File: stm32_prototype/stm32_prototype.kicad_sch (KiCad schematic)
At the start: 16 parts, among them SW1 SW_SPDT, U1 STM32F103C8Tx, Y1 16Mhz

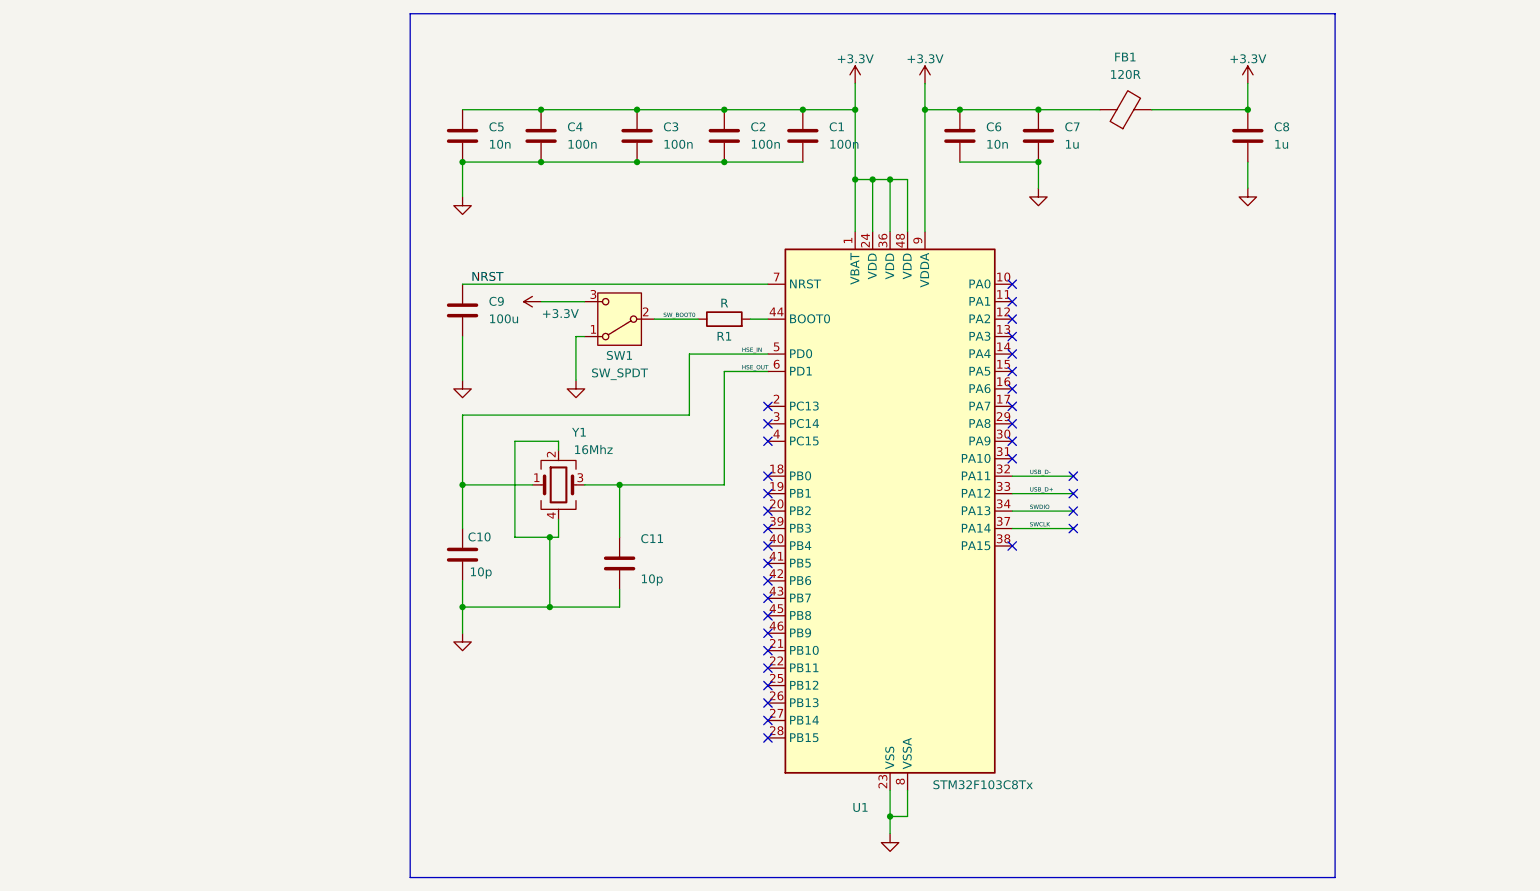
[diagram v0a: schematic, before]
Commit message: Rev B schematic: hierarchical sheets with USB-C, LDO, ESD, debug, Qwiic, Blue-Pill headers
- Split into mcu / power_usb / connectors sheets
- MCU: 8 MHz HSE (15 pF), optional LSE (DNP), BOOT0/RESET buttons, BOOT1 pull-down,
  NRST 100 nF (was 100 uF), VDDA on its own net behind FB1, VBAT solder jumper
- USB-C device (5.1k CC), USBLC6-2SC6, 500 mA PTC, B5819W, AP2112K-3.3
- Cortex-Debug 10-pin, SWD 1x4, Qwiic with jumper-cut 4.7k pull-ups, 2x 1x20 headers
- Footprints, LCSC and MPN on every part; ERC 0 errors / 0 warnings

Co-Authored-By: Claude Opus 5.5 (1M context) <noreply@anthropic.com>
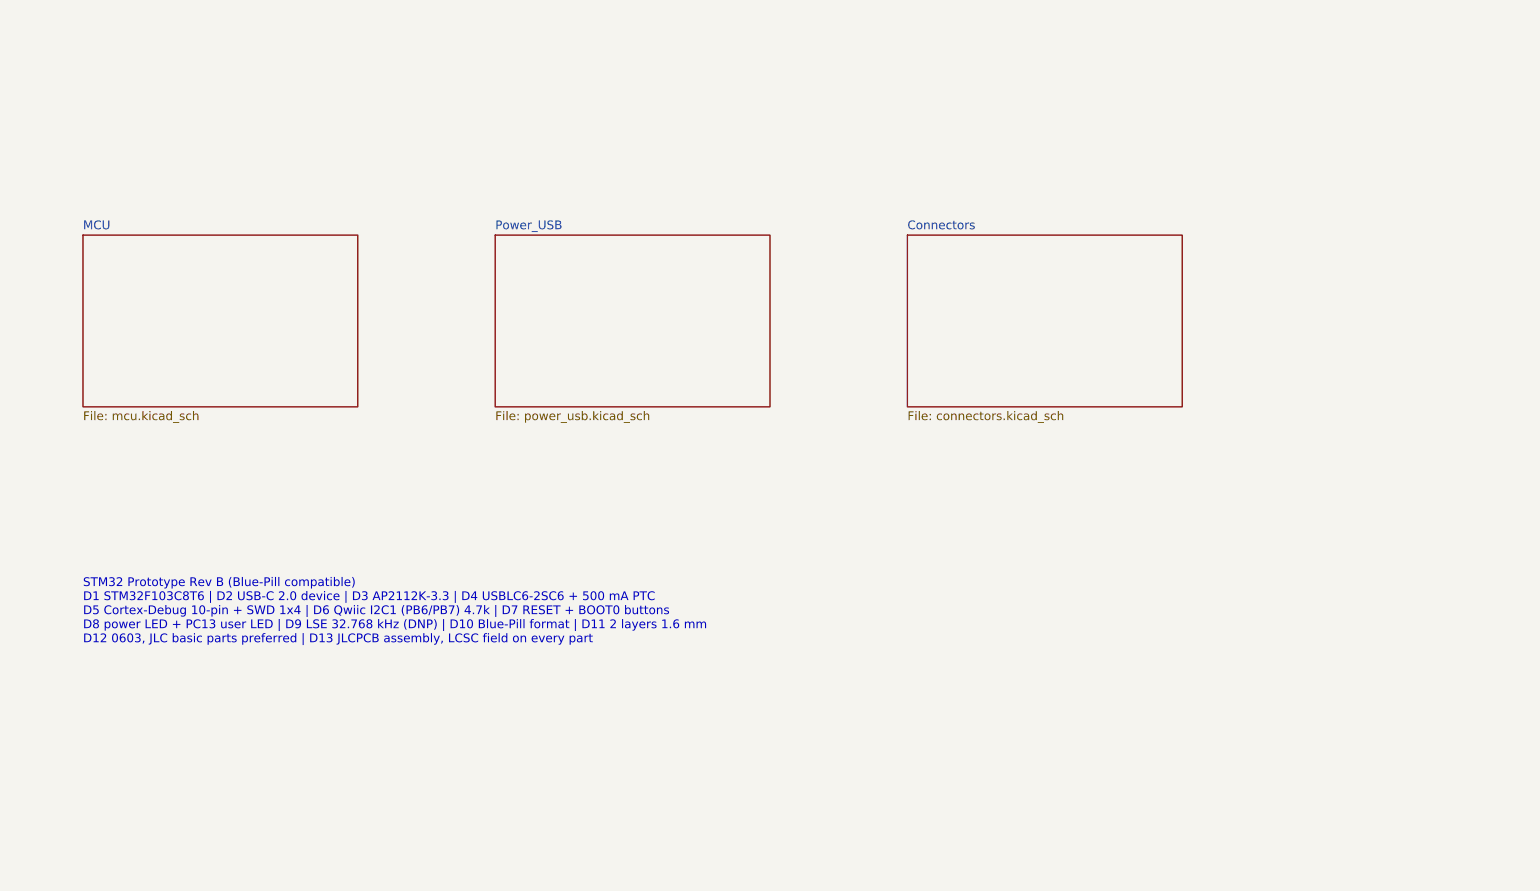
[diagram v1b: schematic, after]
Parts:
- removed C1, C2, C3, C4: 100n, symbol Device:C
- removed C10, C11: 10p, symbol Device:C
- removed C5, C6: 10n, symbol Device:C
- removed C7, C8: 1u, symbol Device:C
- removed C9: 100u, symbol Device:C
- removed FB1: 120R, symbol Device:FerriteBead
- removed R1: R, symbol Device:R
- removed SW1: SW_SPDT, symbol Switch:SW_SPDT
- removed U1: STM32F103C8Tx, Package_QFP:LQFP-48_7x7mm_P0.5mm, symbol MCU_ST_STM32F1:STM32F103C8Tx
- removed Y1: 16Mhz, symbol Device:Crystal_GND24
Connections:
- no-connect marks 35 -> 0
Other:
- added sheet Connectors (connectors.kicad_sch)
- added sheet MCU (mcu.kicad_sch)
- added sheet Power_USB (power_usb.kicad_sch)
- note added: "STM32 Prototype Rev B (Blue-Pill compatible) D1 STM32F103C8T6 | D2 USB-C 2.0 device | D3 AP2112K-3.3 | D4 USBLC6-2SC6 + 500 mA PTC D5 Cortex-Debug 10-pin + SWD 1x4 | D6 Qwiic I2C1 (PB6/PB7) 4.7k | D7 RESET + BOOT0 buttons D8 power LED + PC13 user LED | D9 LSE 32.768 kHz (DNP) | D10 Blue-Pill format | D11 2 layers 1.6 mm D12 0603, JLC basic parts preferred | D13 JLCPCB assembly, LCSC field on ever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"
- title: A prototype for STM32 Bluepill -> STM32 Prototype (Blue Pill) Rev B

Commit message: Rev C schematic: STM32 RC-car controller
- New sheets power / drive / io replace power_usb / connectors
- 2S-3S battery on XT30 with AO4407A reverse protection, SMAJ15A, VBAT sense divider
- TPS563201 5 V / 3 A buck for servos and receiver; logic 5 V ORed from servo rail and USB
- DRV8870 brushed motor driver (3.3 A trip), 4 servo/ESC outputs, 3 receiver inputs,
  2 low-side light outputs, LSM6DS3TR-C IMU on I2C2, UART and 2x5 expansion header
- Project symbol library rcboard.kicad_sym (DRV8870, AO4407A)
- ERC 0/0, netlist matches all 74 intended nets (scripts/revc_schematic)

Co-Authored-By: Claude Opus 5.5 (1M context) <noreply@anthropic.com>
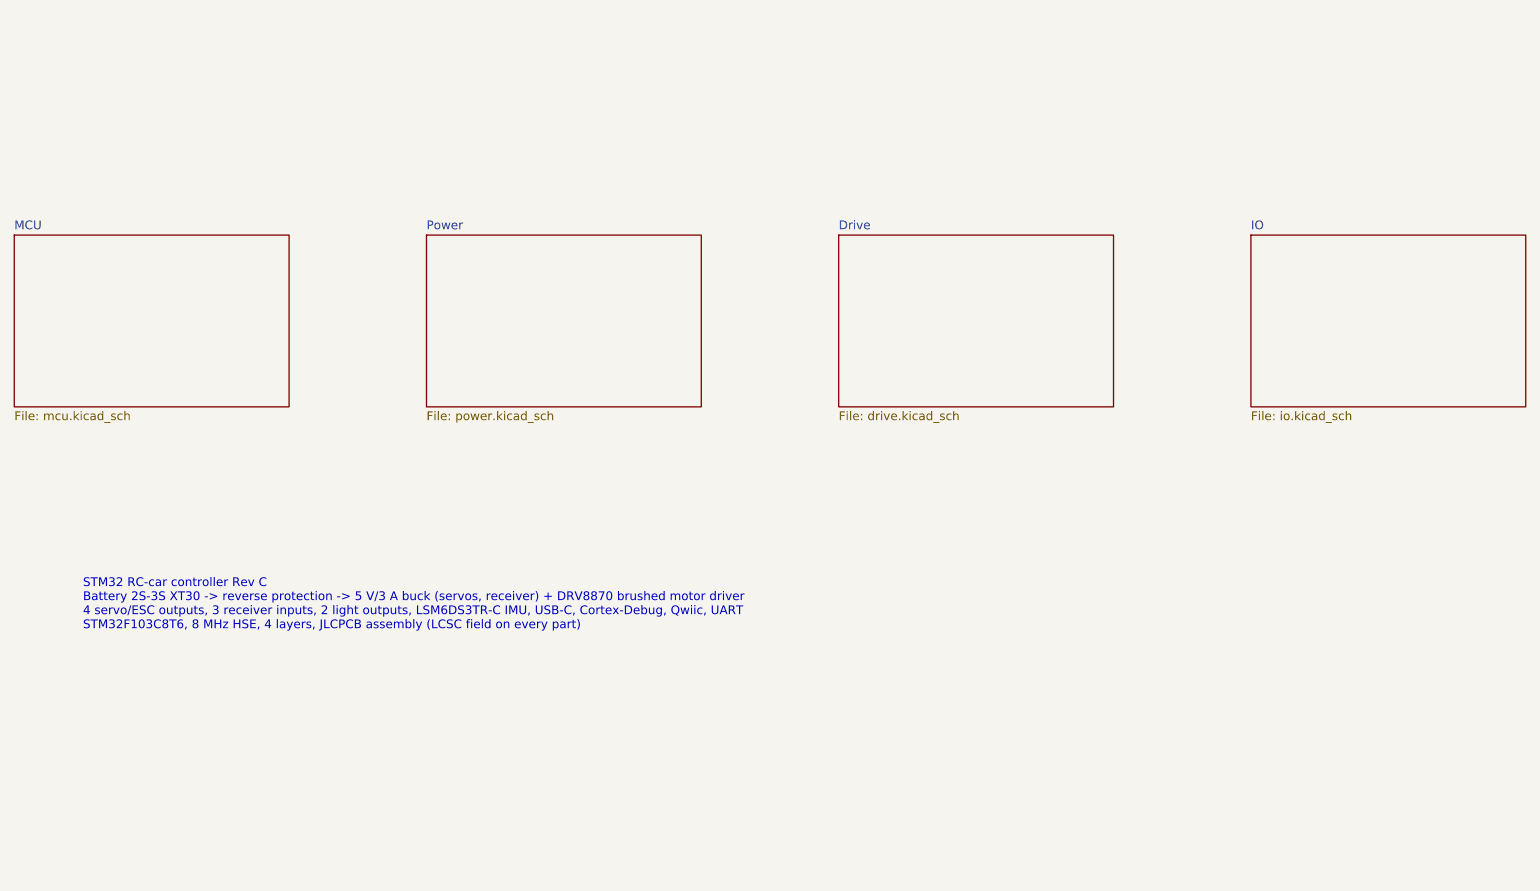
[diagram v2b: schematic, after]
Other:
- removed sheet Connectors
- removed sheet Power_USB
- added sheet Drive (drive.kicad_sch)
- added sheet IO (io.kicad_sch)
- added sheet Power (power.kicad_sch)
- note added: "STM32 RC-car controller Rev C Battery 2S-3S XT30 -> reverse protection -> 5 V/3 A buck (servos, receiver) + DRV8870 brushed motor driver 4 servo/ESC outputs, 3 receiver inputs, 2 light outputs, LSM6DS3TR-C IMU, USB-C, Cortex-Debug, Qwiic, UART STM32F103C8T6, 8 MHz HSE, 4 layers, JLCPCB assembly (LCSC field on every part)"
- note removed: "STM32 Prototype Rev B (Blue-Pill compatible) D1 STM32F103C8T6 | D2 USB-C 2.0 device | D3 AP2112K-3.3 | D4 USBLC6-2SC6 + 500 mA PTC D5 Cortex-Debug 10-pin + SWD 1x4 | D6 Qwiic I2C1 (PB6/PB7) 4.7k | D7 RESET + BOOT0 buttons D8 power LED + PC13 user LED | D9 LSE 32.768 kHz (DNP) | D10 Blue-Pill format | D11 2 layers 1.6 mm D12 0603, JLC basic parts preferred | D13 JLCPCB assembly, LCSC field on ever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"
- title: STM32 Prototype (Blue Pill) Rev B -> STM32 RC-car controller Rev C
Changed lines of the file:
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@@
 	(paper "A4")
 	(title_block
-		(title "STM32 Prototype (Blue Pill) Rev B")
+		(title "STM32 RC-car controller Rev C")
 		(date "2026-10-10")
-		(rev "B")
+		(rev "C")
 		(company "Cagri Catik")
 	)
-	(text "STM32 Prototype Rev B (Blue-Pill compatible)\nD1 STM32F103C8T6 | D2 USB-C 2.0 device | D3 AP2112K-3.3 | D4 USBLC6-2SC6 + 500 mA PTC\nD5 Cortex-Debug 10-pin + SWD 1x4 | D6 Qwiic I2C1 (PB6/PB7) 4.7k | D7 RESET + BOOT0 buttons\nD8 power LED + PC13 user LED | D9 LSE 32.768 kHz (DNP) | D10 Blue-Pill format | D11 2 layers 1.6 mm\nD12 0603, JLC basic parts preferred | D13 JLCPCB assembly, LCSC field on every part"
+	(text "STM32 RC-car controller Rev C\nBattery 2S-3S XT30 -> reverse protection -> 5 V/3 A buck (servos, receiver) + DRV8870 brushed motor driver\n4 servo/ESC outputs, 3 receiver inputs, 2 light outputs, LSM6DS3TR-C IMU, USB-C, Cortex-Debug, Qwiic, UART\nSTM32F103C8T6, 8 MHz HSE, 4 layers, JLCPCB assembly (LCSC field on every part)"
 		(exclude_from_sim no)
 		(at 40 100 0)
@@
 	)
 	(sheet
-		(at 160 50)
+		(at 30 50)
 		(size 40 25)
 		(exclude_from_sim no)
@@
 			(color 0 0 0 0)
 		)
-		(property "Sheetname" "Connectors"
-			(at 160 49.3 0)
+		(property "Sheetname" "MCU"
+			(at 30 49.3 0)
 			(show_name no)
 			(do_not_autoplace no)
@@
 			)
 		)
-		(property "Sheetfile" "connectors.kicad_sch"
-			(at 160 75.6 0)
+		(property "Sheetfile" "mcu.kicad_sch"
+			(at 30 75.6 0)
+			(show_name no)
+			(do_not_autoplace no)
+			(effects
+				(font
+					(size 1.27 1.27)
+				)
+				(justify left top)
+			)
+		)
+		(instances
+			(project "stm32_prototype"
+				(path "/be055fee-c3a5-4e5c-a361-2a24d1729bc4"
+					(page "2")
+				)
+			)
+		)
+	)
+	(sheet
+		(at 210 50)
+		(size 40 25)
+		(exclude_from_sim no)
+		(in_bom yes)
+		(on_board yes)
+		(dnp no)
+		(fields_autoplaced yes)
+		(stroke
+			(width 0.1524)
+			(type solid)
+		)
+		(fill
+			(color 0 0 0 0)
+		)
+		(property "Sheetname" "IO"
+			(at 210 49.3 0)
+			(show_name no)
+			(do_not_autoplace no)
+			(effects
+				(font
+					(size 1.27 1.27)
+				)
+				(justify left bottom)
+			)
+		)
+		(property "Sheetfile" "io.kicad_sch"
+			(at 210 75.6 0)
+			(show_name no)
+			(do_not_autoplace no)
+			(effects
+				(font
+					(size 1.27 1.27)
+				)
+				(justify left top)
+			)
+		)
+		(instances
+			(project "stm32_prototype"
+				(path "/be055fee-c3a5-4e5c-a361-2a24d1729bc4"
+					(page "5")
+				)
+			)
+		)
+	)
+	(sheet
+		(at 150 50)
+		(size 40 25)
+		(exclude_from_sim no)
+		(in_bom yes)
+		(on_board yes)
+		(dnp no)
+		(fields_autoplaced yes)
+		(stroke
+			(width 0.1524)
+			(type solid)
+		)
+		(fill
+			(color 0 0 0 0)
+		)
+		(property "Sheetname" "Drive"
+			(at 150 49.3 0)
+			(show_name no)
+			(do_not_autoplace no)
+			(effects
+				(font
+					(size 1.27 1.27)
+				)
+				(justify left bottom)
+			)
+		)
+		(property "Sheetfile" "drive.kicad_sch"
+			(at 150 75.6 0)
 			(show_name no)
 			(do_not_autoplace no)
@@
 	)
 	(sheet
-		(at 40 50)
+		(at 90 50)
 		(size 40 25)
 		(exclude_from_sim no)
@@
 			(color 0 0 0 0)
 		)
-		(property "Sheetname" "MCU"
-			(at 40 49.3 0)
+		(property "Sheetname" "Power"
+			(at 90 49.3 0)
 			(show_name no)
 			(do_not_autoplace no)
@@
 			)
 		)
-		(property "Sheetfile" "mcu.kicad_sch"
-			(at 40 75.6 0)
+		(property "Sheetfile" "power.kicad_sch"
+			(at 90 75.6 0)
 			(show_name no)
 			(do_not_autoplace no)
-			(effects
-				(font
-					(size 1.27 1.27)
-				)
-				(justify left top)
-			)
-		)
-		(instances
-			(project "stm32_prototype"
-				(path "/be055fee-c3a5-4e5c-a361-2a24d1729bc4"
-					(page "2")
-				)
-			)
-		)
-	)
-	(sheet
-		(at 100 50)
-		(size 40 25)
-		(exclude_from_sim no)
-		(in_bom yes)
-		(on_board yes)
-		(dnp no)
-		(fields_autoplaced yes)
-		(stroke
-			(width 0.1524)
-			(type solid)
-		)
-		(fill
-			(color 0 0 0 0)
-		)
-		(property "Sheetname" "Power_USB"
-			(at 100 49.3 0)
-			(show_name no)
-			(do_not_autoplace no)
-			(effects
-				(font
-					(size 1.27 1.27)
-				)
-				(justify left bottom)
-			)
-		)
-		(property "Sheetfile" "power_usb.kicad_sch"
-			(at 100 75.6 0)
-			(show_name no)
-			(do_not_autoplace no)
